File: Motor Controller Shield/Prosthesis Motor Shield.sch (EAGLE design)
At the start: 46 parts, among them M1_ACT M02PTH, M2_ACT M02PTH

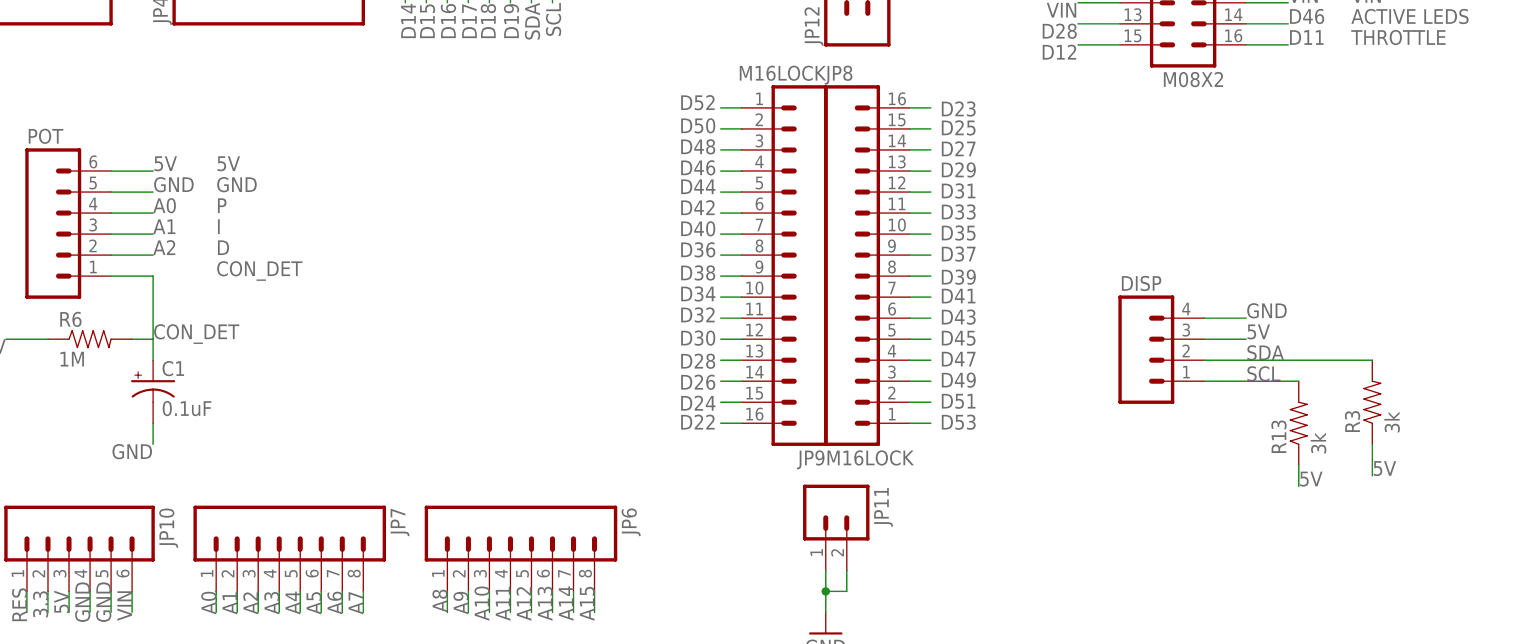
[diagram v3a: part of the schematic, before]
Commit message: Routed motor controller arduino shield. Challenging!
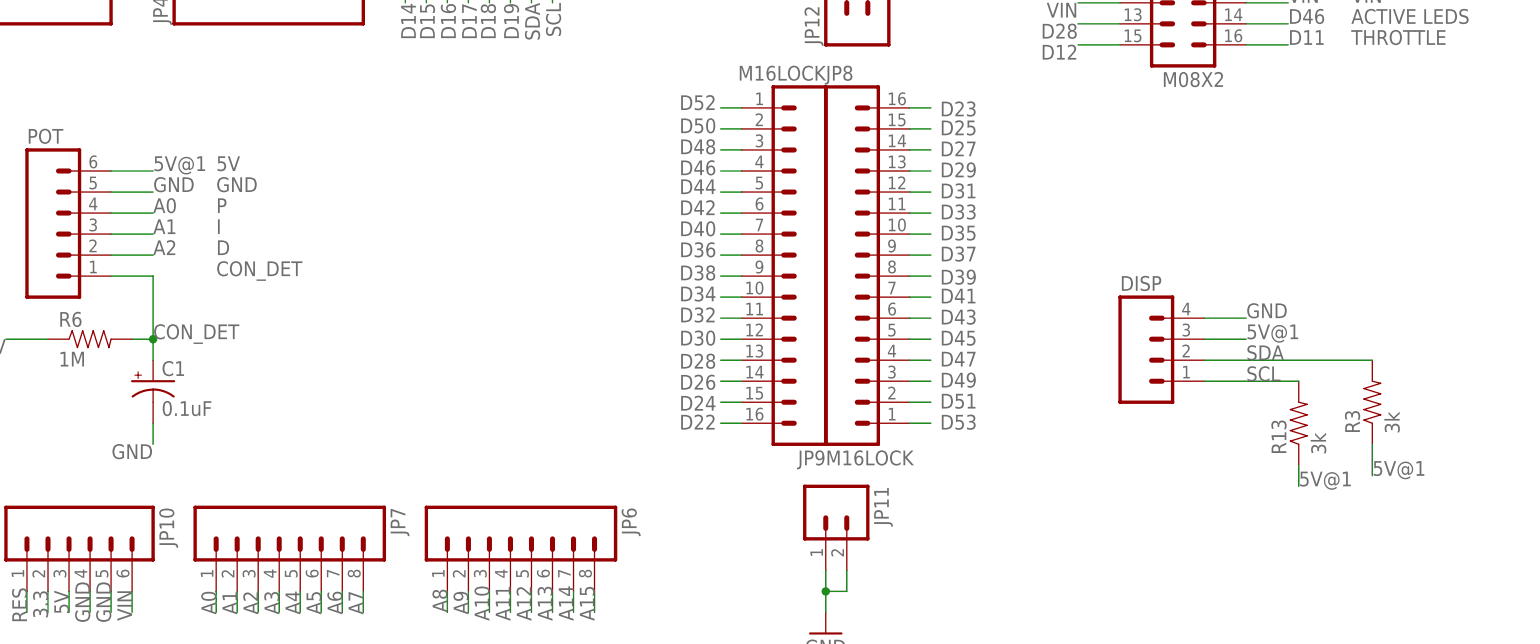
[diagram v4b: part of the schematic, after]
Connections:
- net 5V: no longer DISP.3, POT.6, R13.1, R3.1
- net 5V@1: now also DISP.3, POT.6, R13.1, R3.1
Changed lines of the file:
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@@
 <?xml version="1.0" encoding="utf-8"?>
 <!DOCTYPE eagle SYSTEM "eagle.dtd">
-<eagle version="6.4">
+<eagle version="6.5.0">
 <drawing>
 <settings>
@@
 </segment>
 <segment>
-<wire x1="91.44" y1="106.68" x2="96.52" y2="106.68" width="0.2032" layer="91"/>
-<label x="96.52" y="106.68" size="1.778" layer="95"/>
-<pinref part="POT" gate="G$1" pin="6"/>
-</segment>
-<segment>
 <pinref part="74VHC14MTCX" gate="A" pin="VCC"/>
 <wire x1="99.06" y1="175.26" x2="96.52" y2="175.26" width="0.2032" layer="91"/>
@@
 <wire x1="96.52" y1="223.52" x2="93.98" y2="223.52" width="0.2032" layer="91"/>
 <junction x="96.52" y="223.52"/>
-</segment>
-<segment>
-<pinref part="DISP" gate="G$1" pin="3"/>
-<wire x1="223.52" y1="86.36" x2="228.6" y2="86.36" width="0.2032" layer="91"/>
-<label x="228.6" y="86.36" size="1.778" layer="95"/>
-</segment>
-<segment>
-<pinref part="R3" gate="G$1" pin="1"/>
-<wire x1="243.84" y1="73.66" x2="243.84" y2="69.85" width="0.2032" layer="91"/>
-<label x="243.84" y="69.85" size="1.778" layer="95"/>
-</segment>
-<segment>
-<pinref part="R13" gate="G$1" pin="1"/>
-<wire x1="234.95" y1="71.12" x2="234.95" y2="68.58" width="0.2032" layer="91"/>
-<label x="234.95" y="68.58" size="1.778" layer="95"/>
 </segment>
 </net>
@@
 <label x="208.28" y="137.16" size="1.778" layer="95" rot="R180"/>
 </segment>
+<segment>
+<pinref part="R13" gate="G$1" pin="1"/>
+<wire x1="234.95" y1="71.12" x2="234.95" y2="68.58" width="0.2032" layer="91"/>
+<label x="234.95" y="68.58" size="1.778" layer="95"/>
+</segment>
+<segment>
+<pinref part="R3" gate="G$1" pin="1"/>
+<wire x1="243.84" y1="73.66" x2="243.84" y2="69.85" width="0.2032" layer="91"/>
+<label x="243.84" y="69.85" size="1.778" layer="95"/>
+</segment>
+<segment>
+<pinref part="DISP" gate="G$1" pin="3"/>
+<wire x1="223.52" y1="86.36" x2="228.6" y2="86.36" width="0.2032" layer="91"/>
+<label x="228.6" y="86.36" size="1.778" layer="95"/>
+</segment>
+<segment>
+<wire x1="91.44" y1="106.68" x2="96.52" y2="106.68" width="0.2032" layer="91"/>
+<label x="96.52" y="106.68" size="1.778" layer="95"/>
+<pinref part="POT" gate="G$1" pin="6"/>
+</segment>
 </net>
 <net name="D22" class="0">
@@
 <pinref part="C1" gate="G$1" pin="+"/>
 <wire x1="96.52" y1="86.36" x2="96.52" y2="83.82" width="0.2032" layer="91"/>
-</segment>
-<segment>
+<junction x="96.52" y="86.36"/>
+</segment>
+<segment>
